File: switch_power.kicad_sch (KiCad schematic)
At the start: 79 parts, among them Y1 Crystal_GND24

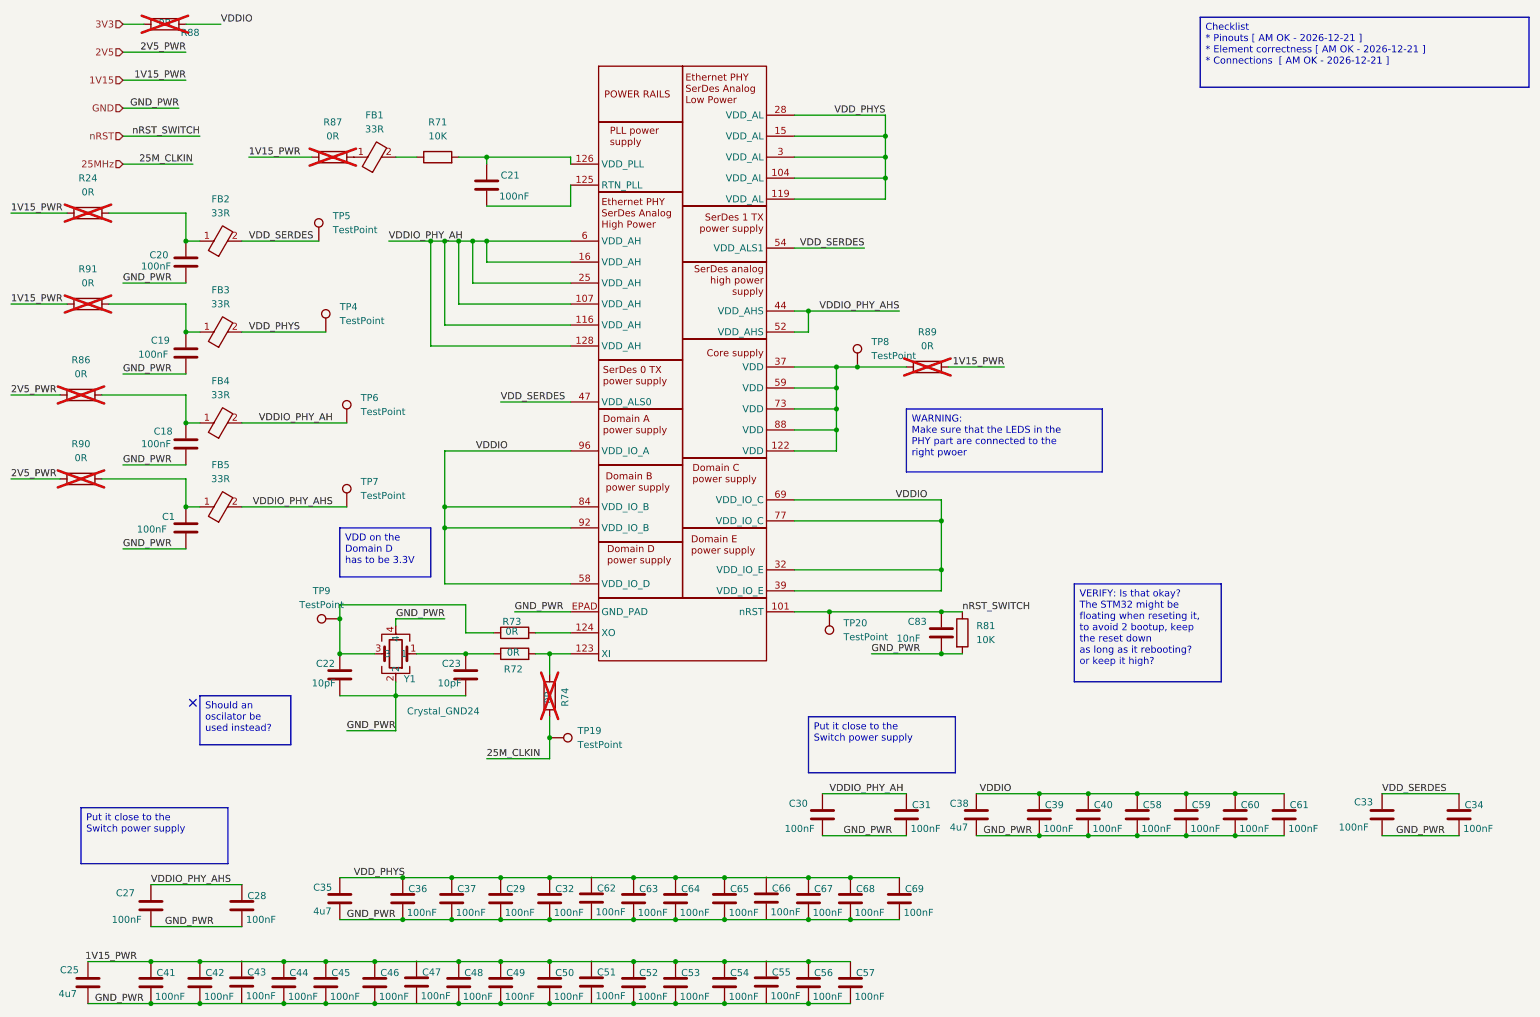
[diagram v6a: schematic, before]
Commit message: fixing issue related to symbol changes, and updating components
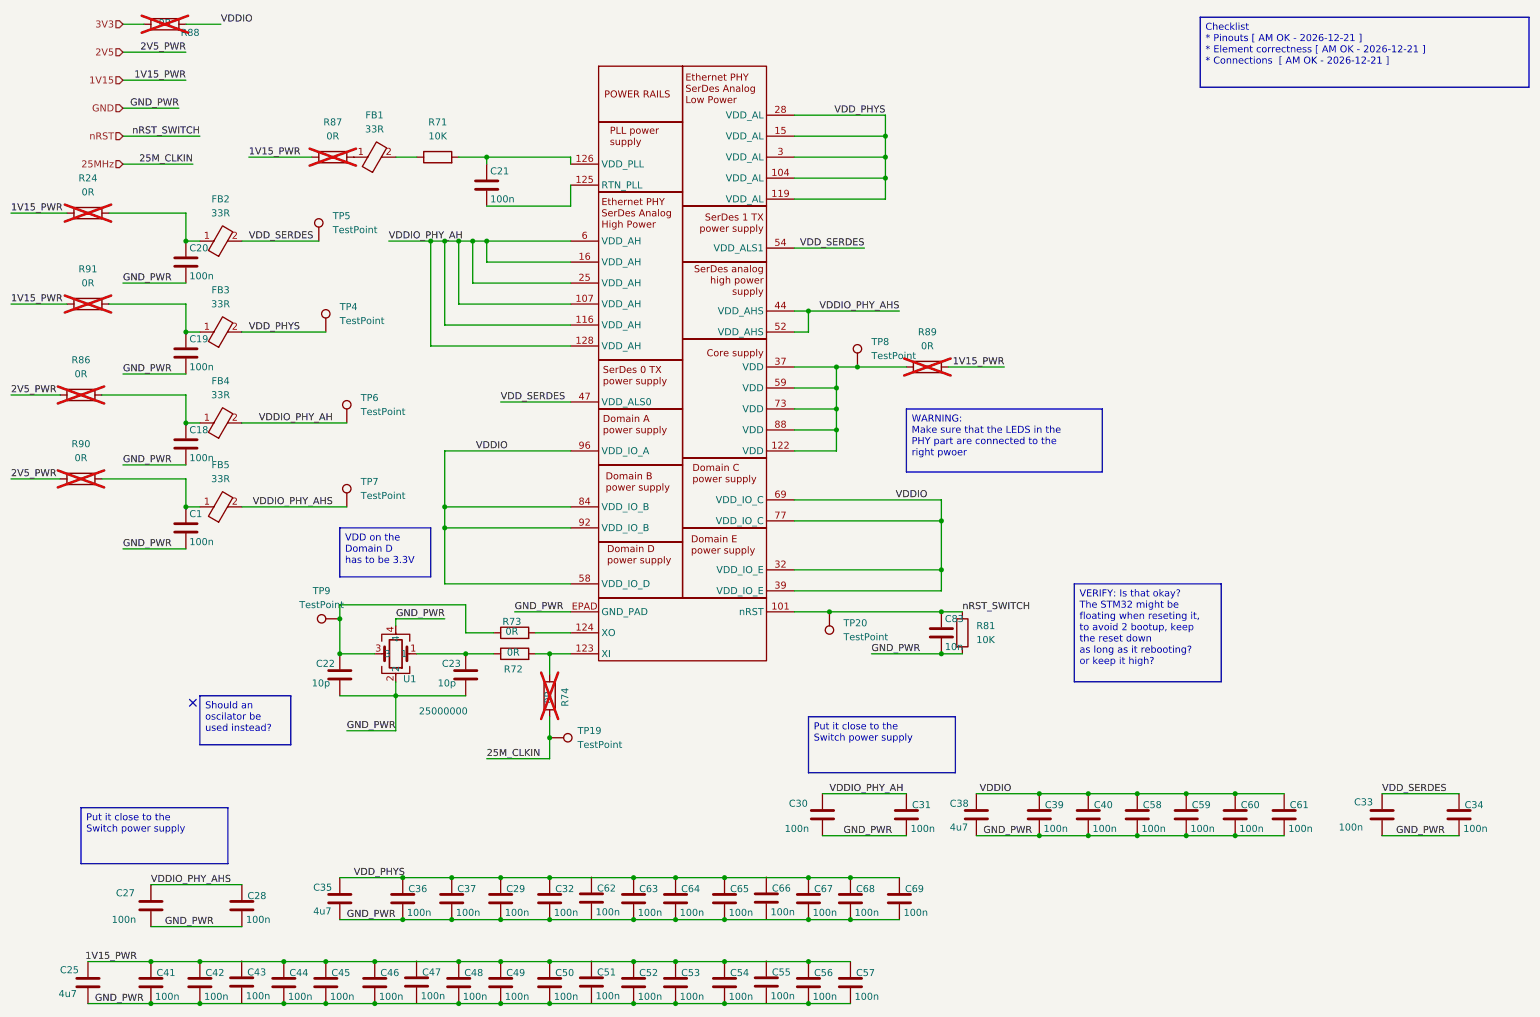
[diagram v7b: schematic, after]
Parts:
- C1, C18, C19, C20, C21: value 100nF -> 100n; footprint KL:C_0402 -> Capacitor_SMD:C_0201_0603Metric; symbol KL_C:C_100nF_35V_X7R_0402_10 -> KL_C:C_100n_35V_X7R_402_10
- C22, C23: value 10pF -> 10p; footprint KL:C_0603 -> Capacitor_SMD:C_0201_0603Metric; symbol KL_C:C_10pF_25V_C0G_0603_5 -> KL_C:C_10p_25V_C0G_0603_5
- C25, C35, C38: footprint KL:C_0603 -> Capacitor_SMD:C_0201_0603Metric
- C27, C28, C29, C30, C31, C32, C33, C34, C36, C37, C39, C40, C41, C42, C43, C44, C45, C46, C47, C48, C49, C50, C51, C52, C53, C54, C55, C56, C57, C58, C59, C60, C61, C62, C63, C64, C65, C66, C67, C68, C69: value 100nF -> 100n; footprint KL:C_0603 -> Capacitor_SMD:C_0201_0603Metric; symbol KL_C:C_100nF_16V_X7R_0603_10 -> KL_C:C_100n_16V_X7R_0603_10
- C83: value 10nF -> 10n; footprint KL:C_0603 -> Capacitor_SMD:C_0201_0603Metric; symbol KL_C:C_10nF_25V_X7R_0603_20 -> KL_C:C_10n_50V_X7R_0603_10; Digikey 311-3111-1-ND -> 1276-CL10B103KB8WPNDCT-ND; LCSC C726559 -> C307346; Mouser 603-AC603KRX7R8BB103 -> 187-CL10B103KB8WPND; Tolerance 20 -> 10; Voltage 25 -> 50
- FB1, FB2, FB3, FB4, FB5: symbol KL_Ferrites:KL_FerritBead_33_3A -> KL_Ferrites:KL_FerritBead_33_3
- R71, R72, R73, R74, R81: footprint KL:R_0603 -> KL_Footprints:C_0603
- U1: renamed from Y1; value Crystal_GND24 -> 25000000; symbol KL_Passive_ICs:Crystal_25MHz_32pF -> KL_Passive_ICs:Crystal_25MHz_32p

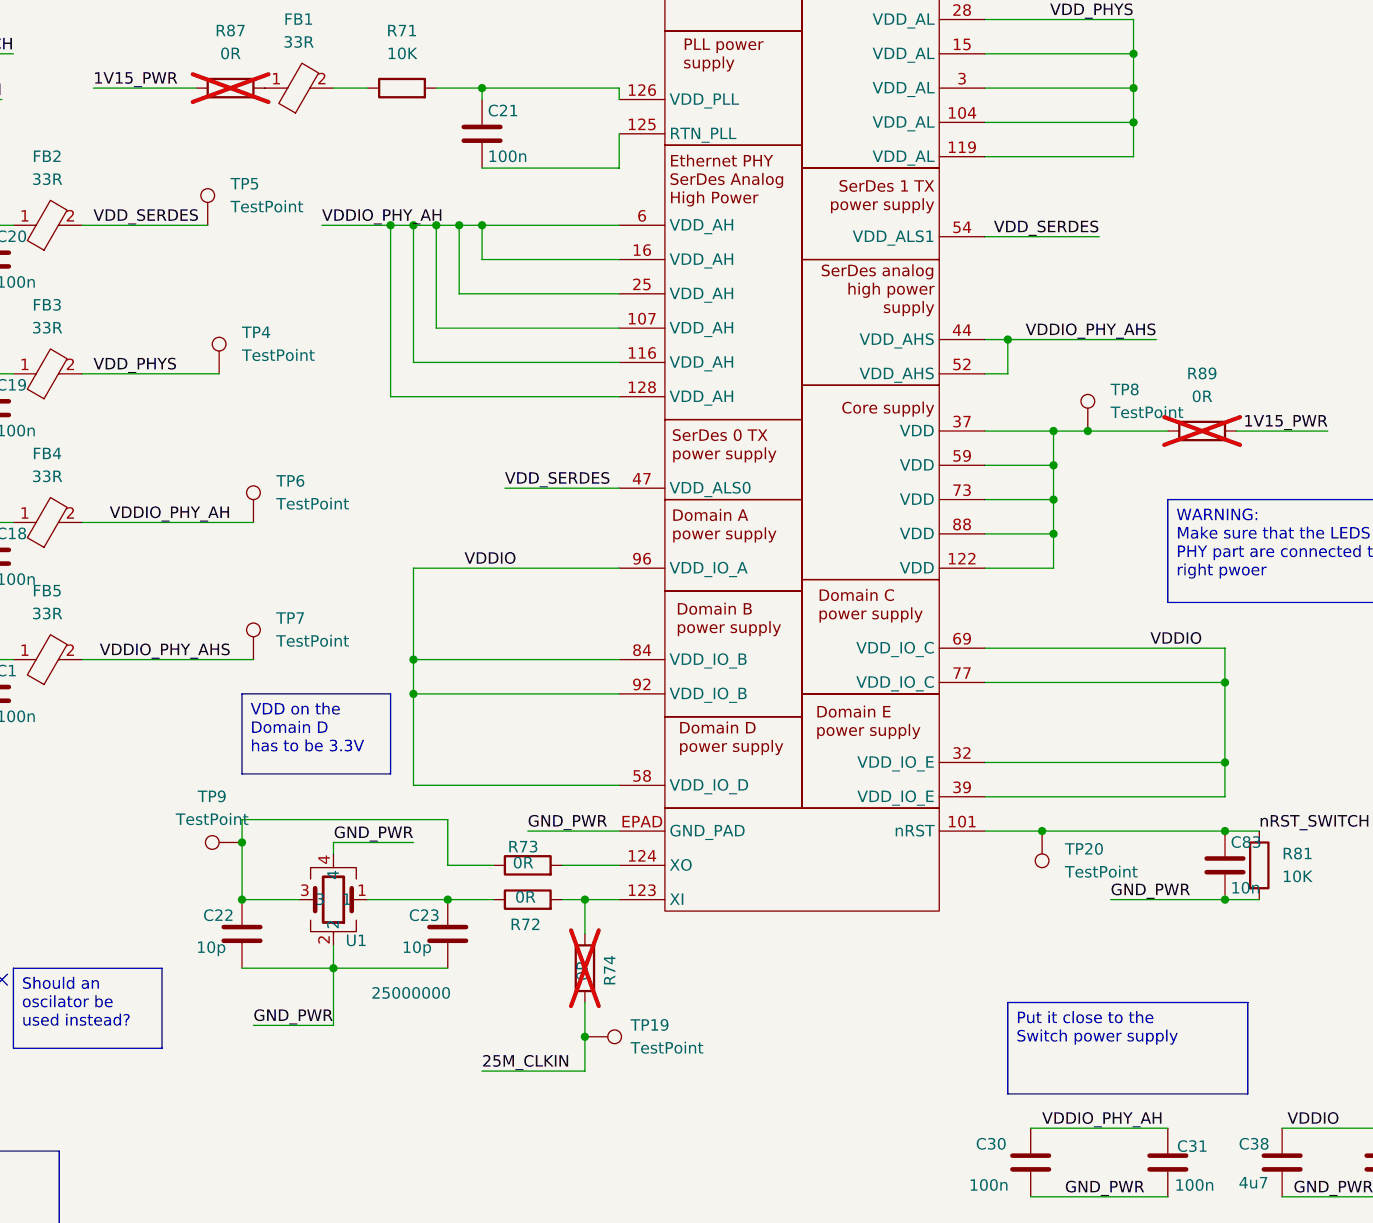
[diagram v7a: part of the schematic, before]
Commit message: updates test points
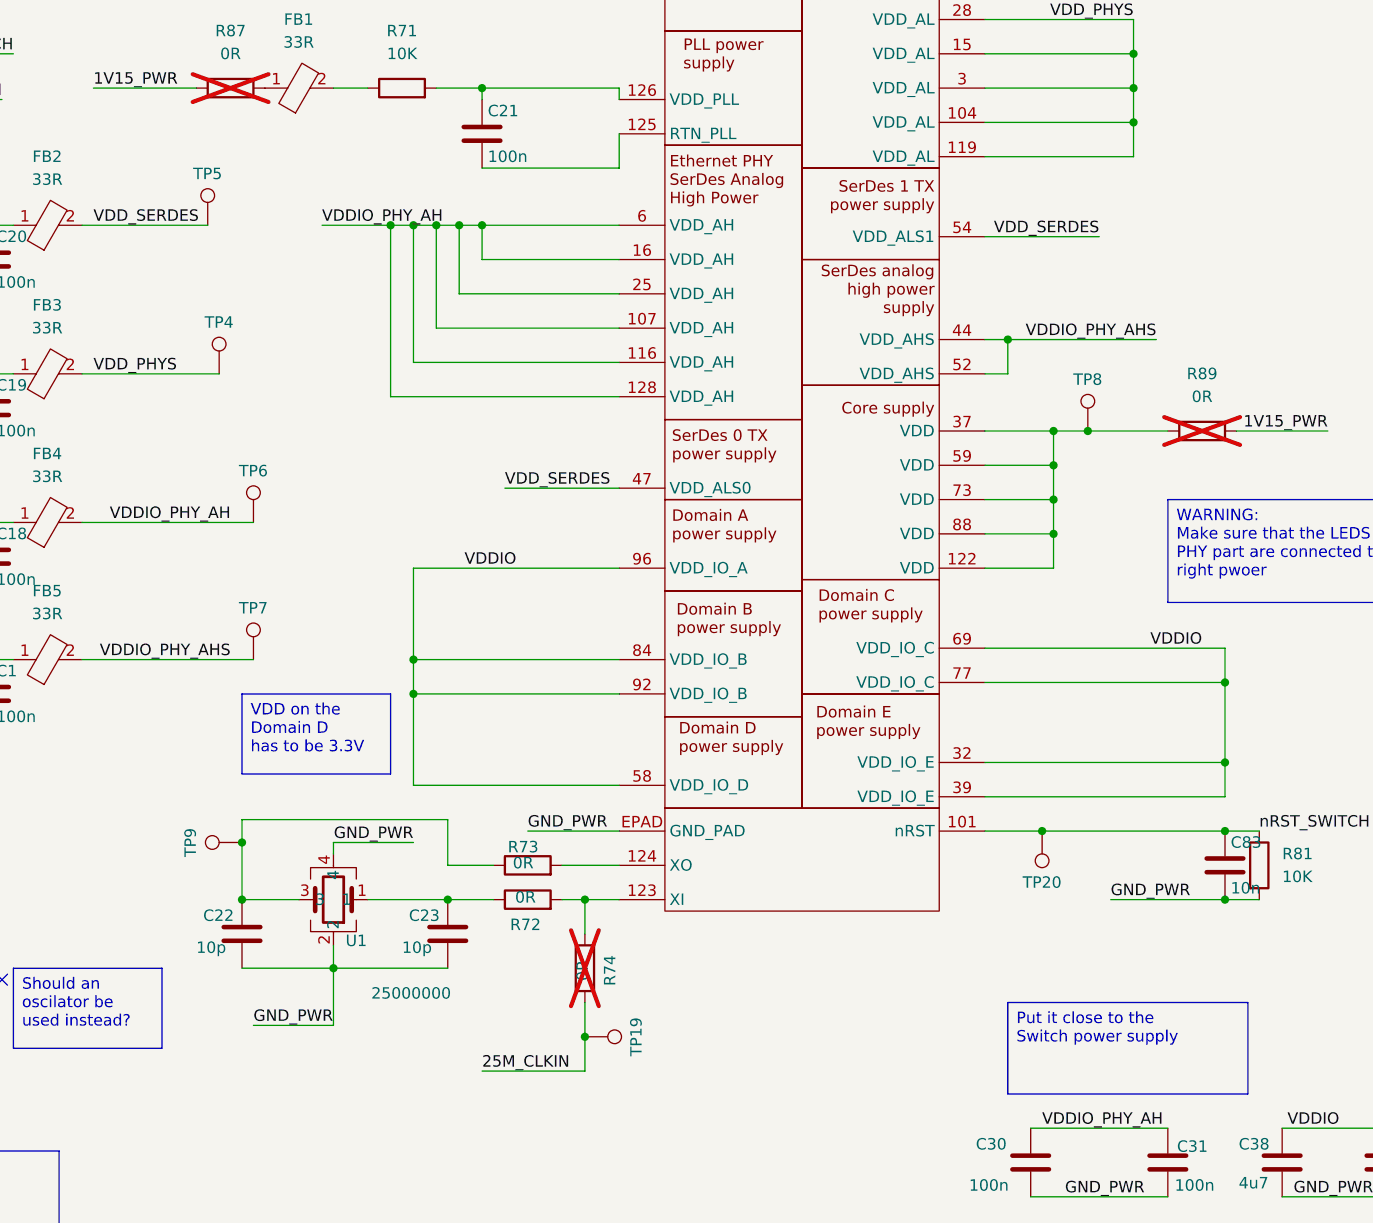
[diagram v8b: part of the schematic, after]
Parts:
- TP19, TP20, TP4, TP5, TP6, TP7, TP8, TP9: value TestPoint -> (none); footprint (none) -> Connector_PinHeader_2.54mm:PinHeader_1x01_P2.54mm_Vertical; symbol Connector:TestPoint -> KL_TP:TestPoint
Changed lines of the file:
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@@
 	)
 	(symbol
-		(lib_id "Connector:TestPoint")
+		(lib_id "KL_TP:TestPoint")
 		(at 161.29 77.47 0)
 		(unit 1)
@@
 		(fields_autoplaced yes)
 		(property "Reference" "TP8"
-			(at 163.83 72.8979 0)
+			(at 161.29 71.755 0)
+			(do_not_autoplace yes)
 			(effects
 				(font
 					(size 1.27 1.27)
 				)
-				(justify left)
 			)
 		)
-		(property "Value" "TestPoint"
-			(at 163.83 75.4379 0)
+		(property "Value" ""
+			(at 161.29 72.39 0)
 			(effects
 				(font
 					(size 1.27 1.27)
 				)
-				(justify left)
+				(hide yes)
 			)
 		)
-		(property "Footprint" ""
+		(property "Footprint" "Connector_PinHeader_2.54mm:PinHeader_1x01_P2.54mm_Vertical"
 			(at 166.37 77.47 0)
 			(effects
@@
 	)
 	(symbol
-		(lib_id "Connector:TestPoint")
+		(lib_id "KL_TP:TestPoint")
 		(at 67.31 123.19 90)
 		(unit 1)
@@
 		(fields_autoplaced yes)
 		(property "Reference" "TP9"
-			(at 64.008 118.11 90)
+			(at 61.595 123.19 0)
+			(do_not_autoplace yes)
 			(effects
 				(font
@@
 			)
 		)
-		(property "Value" "TestPoint"
-			(at 64.008 120.65 90)
+		(property "Value" ""
+			(at 62.23 123.19 0)
 			(effects
 				(font
 					(size 1.27 1.27)
 				)
+				(hide yes)
 			)
 		)
-		(property "Footprint" ""
+		(property "Footprint" "Connector_PinHeader_2.54mm:PinHeader_1x01_P2.54mm_Vertical"
 			(at 67.31 118.11 0)
 			(effects
@@
 	)
 	(symbol
-		(lib_id "Connector:TestPoint")
+		(lib_id "KL_TP:TestPoint")
 		(at 63.5 54.61 0)
 		(unit 1)
@@
 		(fields_autoplaced yes)
 		(property "Reference" "TP5"
-			(at 66.04 50.0379 0)
+			(at 63.5 48.895 0)
+			(do_not_autoplace yes)
 			(effects
 				(font
 					(size 1.27 1.27)
 				)
-				(justify left)
 			)
 		)
-		(property "Value" "TestPoint"
-			(at 66.04 52.5779 0)
+		(property "Value" ""
+			(at 63.5 49.53 0)
 			(effects
 				(font
 					(size 1.27 1.27)
 				)
-				(justify left)
+				(hide yes)
 			)
 		)
-		(property "Footprint" ""
+		(property "Footprint" "Connector_PinHeader_2.54mm:PinHeader_1x01_P2.54mm_Vertical"
 			(at 68.58 54.61 0)
 			(effects
@@
 	)
 	(symbol
-		(lib_id "Connector:TestPoint")
+		(lib_id "KL_TP:TestPoint")
 		(at 68.58 87.63 0)
 		(unit 1)
@@
 		(fields_autoplaced yes)
 		(property "Reference" "TP6"
-			(at 71.12 83.0579 0)
+			(at 68.58 81.915 0)
+			(do_not_autoplace yes)
 			(effects
 				(font
 					(size 1.27 1.27)
 				)
-				(justify left)
 			)
 		)
-		(property "Value" "TestPoint"
-			(at 71.12 85.5979 0)
+		(property "Value" ""
+			(at 68.58 82.55 0)
 			(effects
 				(font
 					(size 1.27 1.27)
 				)
-				(justify left)
+				(hide yes)
 			)
 		)
-		(property "Footprint" ""
+		(property "Footprint" "Connector_PinHeader_2.54mm:PinHeader_1x01_P2.54mm_Vertical"
 			(at 73.66 87.63 0)
 			(effects
@@
 	)
 	(symbol
-		(lib_id "Connector:TestPoint")
+		(lib_id "KL_TP:TestPoint")
 		(at 156.21 121.92 180)
 		(unit 1)
@@
 		(fields_autoplaced yes)
 		(property "Reference" "TP20"
-			(at 158.75 123.9519 0)
+			(at 156.21 127.635 0)
+			(do_not_autoplace yes)
 			(effects
 				(font
 					(size 1.27 1.27)
 				)
-				(justify right)
 			)
 		)
-		(property "Value" "TestPoint"
-			(at 158.75 126.4919 0)
+		(property "Value" ""
+			(at 156.21 127 0)
 			(effects
 				(font
 					(size 1.27 1.27)
 				)
-				(justify right)
+				(hide yes)
 			)
 		)
-		(property "Footprint" ""
+		(property "Footprint" "Connector_PinHeader_2.54mm:PinHeader_1x01_P2.54mm_Vertical"
 			(at 151.13 121.92 0)
 			(effects
@@
 	)
 	(symbol
-		(lib_id "Connector:TestPoint")
+		(lib_id "KL_TP:TestPoint")
 		(at 68.58 102.87 0)
 		(unit 1)
@@
 		(fields_autoplaced yes)
 		(property "Reference" "TP7"
-			(at 71.12 98.2979 0)
+			(at 68.58 97.155 0)
+			(do_not_autoplace yes)
 			(effects
 				(font
 					(size 1.27 1.27)
 				)
-				(justify left)
 			)
 		)
-		(property "Value" "TestPoint"
-			(at 71.12 100.8379 0)
+		(property "Value" ""
+			(at 68.58 97.79 0)
 			(effects
 				(font
 					(size 1.27 1.27)
 				)
-				(justify left)
+				(hide yes)
 			)
 		)
-		(property "Footprint" ""
+		(property "Footprint" "Connector_PinHeader_2.54mm:PinHeader_1x01_P2.54mm_Vertical"
 			(at 73.66 102.87 0)
 			(effects
@@
 	)
 	(symbol
-		(lib_id "Connector:TestPoint")
+		(lib_id "KL_TP:TestPoint")
 		(at 105.41 144.78 270)
 		(unit 1)
@@
 		(fields_autoplaced yes)
 		(property "Reference" "TP19"
-			(at 110.49 143.5099 90)
+			(at 111.125 144.78 0)
+			(do_not_autoplace yes)
 			(effects
 				(font
 					(size 1.27 1.27)
 				)
-				(justify left)
 			)
 		)
-		(property "Value" "TestPoint"
-			(at 110.49 146.0499 90)
+		(property "Value" ""
+			(at 110.49 144.78 0)
 			(effects
 				(font
 					(size 1.27 1.27)
 				)
-				(justify left)
+				(hide yes)
 			)
 		)
-		(property "Footprint" ""
+		(property "Footprint" "Connector_PinHeader_2.54mm:PinHeader_1x01_P2.54mm_Vertical"
 			(at 105.41 149.86 0)
 			(effects
@@
 	)
 	(symbol
-		(lib_id "Connector:TestPoint")
+		(lib_id "KL_TP:TestPoint")
 		(at 64.77 71.12 0)
 		(unit 1)
@@
 		(fields_autoplaced yes)
 		(property "Reference" "TP4"
-			(at 67.31 66.5479 0)
+			(at 64.77 65.405 0)
+			(do_not_autoplace yes)
 			(effects
 				(font
 					(size 1.27 1.27)
 				)
-				(justify left)
 			)
 		)
-		(property "Value" "TestPoint"
-			(at 67.31 69.0879 0)
+		(property "Value" ""
+			(at 64.77 66.04 0)
 			(effects
 				(font
 					(size 1.27 1.27)
 				)
-				(justify left)
+				(hide yes)
 			)
 		)
-		(property "Footprint" ""
+		(property "Footprint" "Connector_PinHeader_2.54mm:PinHeader_1x01_P2.54mm_Vertical"
 			(at 69.85 71.12 0)
 			(effects
